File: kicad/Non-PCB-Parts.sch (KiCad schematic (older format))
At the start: 1 part

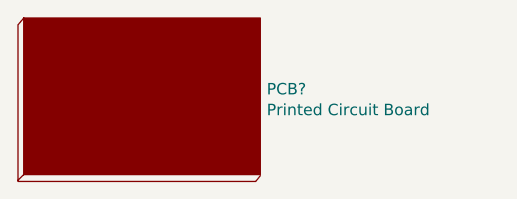
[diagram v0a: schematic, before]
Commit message: Footprint Update
Added Arduino Pro Mini footprint to Module.pretty
Added rats nest to PCB file
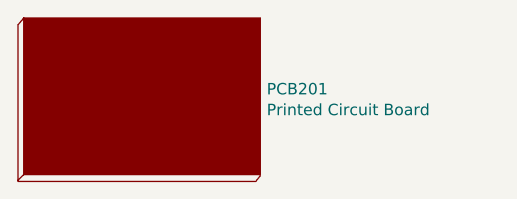
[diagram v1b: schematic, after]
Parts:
- gave numbers to parts that had none: 1
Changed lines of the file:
@@
 $EndDescr
 $Comp
-L special:Circuit_Board PCB?
+L special:Circuit_Board PCB201
 U 1 1 5FCC9970
 P 3150 2350
-F 0 "PCB?" H 3698 2374 50  0000 L CNN
+F 0 "PCB201" H 3698 2374 50  0000 L CNN
 F 1 "Printed Circuit Board" H 3698 2283 50  0000 L CNN
 F 2 "Oddities:Dummy_Empty" H 3990 2510 50  0001 C CNN
